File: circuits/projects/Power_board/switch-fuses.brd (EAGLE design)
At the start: 75 x 50 mm, 22 parts

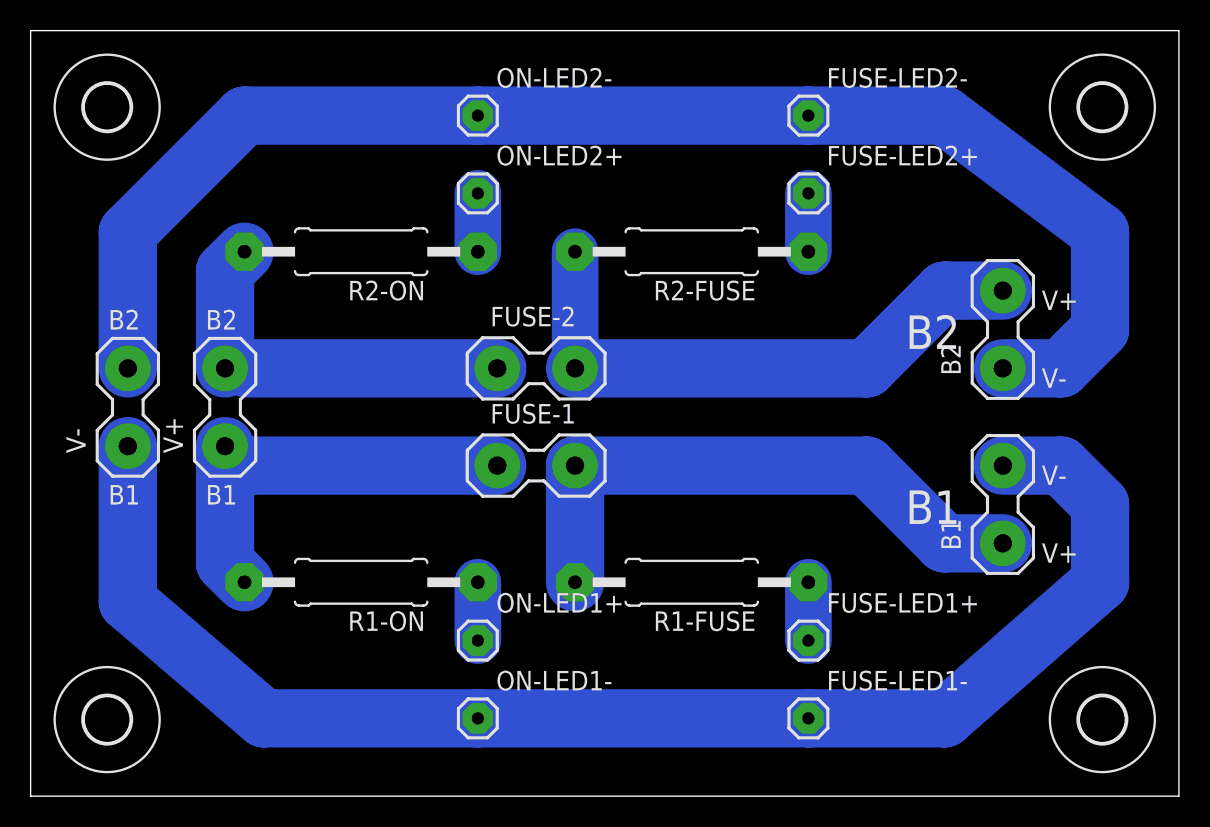
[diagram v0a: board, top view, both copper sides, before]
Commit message: more datasheets
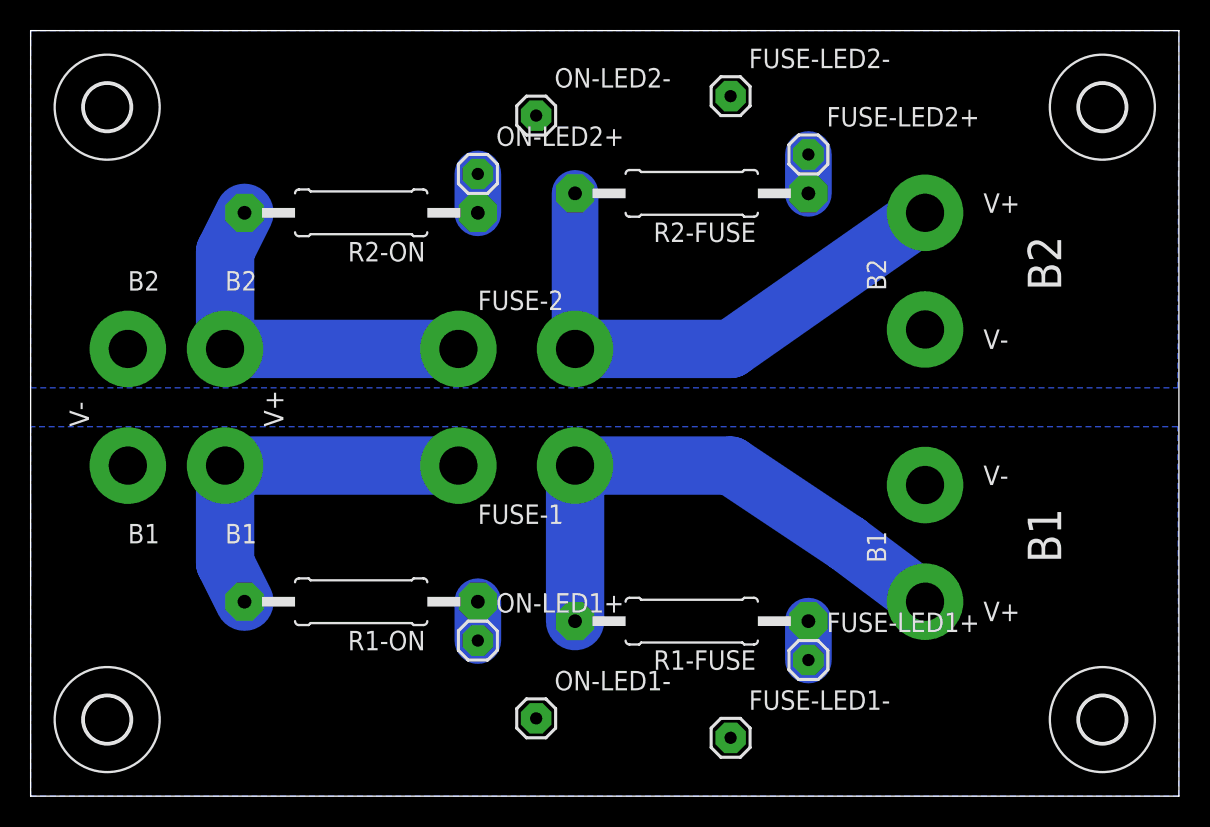
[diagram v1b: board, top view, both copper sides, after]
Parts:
- B1, B2, FUSE-1, FUSE-2, V+, V-: value 2-HOLES2-HOLES-5.08MM -> 2-HOLES2.5MM; device parts:2-HOLES_BIG -> parts:2-HOLE-2.5MM
- FUSE-LED1+, FUSE-LED1-, FUSE-LED2+, FUSE-LED2-, ON-LED1+, ON-LED1-, ON-LED2+, ON-LED2-: value 1-HOLE" -> 1-HOLE0.8MM
- moved B2 6.35 mm to (58.4, 34.3)
- moved B1 5.68 mm to (58.4, 16.5)
- moved FUSE-LED1- 5.24 mm to (45.7, 3.81)
- moved FUSE-LED2- 5.24 mm to (45.7, 45.7)
- moved ON-LED1- 3.81 mm to (33.0, 5.08)
- moved ON-LED2- 3.81 mm to (33.0, 44.5)
- moved R2-FUSE 3.81 mm to (43.2, 39.4)
- moved R1-FUSE 2.54 mm to (43.2, 11.4)
- moved FUSE-LED2+ 2.54 mm to (50.8, 41.9)
- moved R2-ON 2.54 mm to (21.6, 38.1)
- moved FUSE-2 1.80 mm to (31.8, 29.2)
- moved FUSE-1 1.27 mm to (31.8, 21.6)
- moved ON-LED2+ 1.27 mm to (29.2, 40.6)
- moved R1-ON 1.27 mm to (21.6, 12.7)
- moved FUSE-LED1+ 1.27 mm to (50.8, 8.89)
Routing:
- net V-1: track 92.3 -> 0.00 mm
- net V-2: track 91.8 -> 0.00 mm
- net VIN2: track 27.7 -> 24.4 mm
- net V+1: track 37.7 -> 35.8 mm
- net VIN1: track 25.9 -> 24.4 mm
- net V+2: track 38.4 -> 39.7 mm
- net N$9: track 3.81 -> 2.54 mm
- net N$3: track 3.81 -> 2.54 mm
- net N$4: track 3.81 -> 2.54 mm
- net N$10: track 3.81 -> 2.54 mm
- added copper zone on layer 16, net V-1
- added copper zone on layer 16, net V-2

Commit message: made board tracks bigger
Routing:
- net V+2: track 39.7 -> 37.1 mm
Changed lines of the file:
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@@
 <setting verticaltext="up"/>
 </settings>
-<grid distance="0.05" unitdist="inch" unit="mil" style="lines" multiple="1" display="yes" altdistance="0.025" altunitdist="inch" altunit="mil"/>
+<grid distance="25" unitdist="mil" unit="mil" style="lines" multiple="1" display="yes" altdistance="12.5" altunitdist="mil" altunit="mil"/>
 <layers>
 <layer number="1" name="Top" color="4" fill="1" visible="yes" active="yes"/>
@@
 <contactref element="FUSE-2" pad="2"/>
 <contactref element="B2" pad="2"/>
-<wire x1="35.56" y1="29.21" x2="36.83" y2="28.956" width="3.048" layer="16"/>
-<wire x1="36.83" y1="28.956" x2="35.56" y2="29.21" width="3.048" layer="16"/>
 <wire x1="35.56" y1="29.21" x2="35.56" y2="39.37" width="3.048" layer="16"/>
 <wire x1="45.72" y1="29.21" x2="58.42" y2="38.1" width="3.81" layer="16"/>

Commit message: new shit
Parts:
- removed B1, B2, FUSE-1, FUSE-2, V+, V-: 2-HOLES2.5MM, parts:2-HOLE-2.5MM
- added B1_V+, B1_V+OUT, B1_V-, B1_V_OUT, B2_V+, B2_V+OUT, B2_V-, B2_V-OUT, F1_A, F1_B, F2_A, F2_B: 1-HOLE2.5MM, parts:1-HOLE-2.5MM
- moved ON-LED2+ 34.9 mm to (35.6, 6.35)
- moved ON-LED1+ 33.6 mm to (35.6, 43.2)
- moved FUSE-LED2+ 32.2 mm to (45.7, 10.2)
- moved R2-ON 31.8 mm to (22.9, 6.35)
- moved FUSE-LED1+ 30.9 mm to (45.7, 39.4)
- moved R1-ON 30.5 mm to (22.9, 43.2)
- moved R2-FUSE 27.1 mm to (38.1, 12.7)
- moved R1-FUSE 25.9 mm to (38.1, 36.8)
- moved ON-LED1- 10.2 mm to (43.2, 6.35)
- moved ON-LED2- 10.2 mm to (43.2, 44.5)
- moved U$2 10.0 mm to (60.0, 45.0)
- moved U$4 10.0 mm to (60.0, 5.00)
- moved FUSE-LED1- 5.68 mm to (40.6, 6.35)
- moved FUSE-LED2- 5.24 mm to (40.6, 44.5)
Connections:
- net V+1: now also B2_V+OUT.P$1, F2_B.P$1; no longer B1.1, FUSE-1.2
- net V+2: now also B1_V+OUT.P$1, F1_B.P$1; no longer B2.2, FUSE-2.2
- net V-1: now also B1_V-.P$1, B1_V_OUT.P$1; no longer B1.2, V-.1
- net V-2: now also B2_V-.P$1, B2_V-OUT.P$1; no longer B2.1, V-.2
- net VIN1: now also B1_V+.P$1, F1_A.P$1; no longer FUSE-2.1, V+.2
- net VIN2: now also B2_V+.P$1, F2_A.P$1; no longer FUSE-1.1, V+.1
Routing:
- net V+2: track 37.1 -> 12.7 mm
- net V-2: track 0.00 -> 23.5 mm
- net V-1: track 0.00 -> 22.3 mm
- net V+1: track 35.8 -> 14.0 mm
- net VIN1: track 24.4 -> 19.1 mm
- net VIN2: track 24.4 -> 20.3 mm
- net N$9: track 2.54 -> 5.08 mm
- net N$10: track 2.54 -> 5.08 mm
- removed copper zone on layer 16, net V-1
- removed copper zone on layer 16, net V-2
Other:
- board size 75 x 50 mm -> 65 x 50 mm
